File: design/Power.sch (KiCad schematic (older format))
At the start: 50 parts, among them U2 TC2117, U3 DRV8302

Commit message: Saved project with more recent version of KiCad. Added IRS2184 half bridge driver to BLDC_4_cache.lib
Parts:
- C1, C18, C19, C20, C21, C22, C23, C24, C26, C27, C28, C29, C30, C34, C36, C37, C39, C40, C43, C44, C49, C51, C52, C8, C9: symbol C -> C-RESCUE-BLDC_4
- C25, C33: symbol CP1 -> CP1-RESCUE-BLDC_4
- R15, R16, R17, R18, R19, R20, R21, R23, R24, R25, R26, R27, R32, R33, R48, R49, R50, R51: symbol R -> R-RESCUE-BLDC_4
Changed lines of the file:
@@
 EESchema Schematic File Version 2
+LIBS:BLDC_4-rescue
 LIBS:power
 LIBS:device
@@
 LIBS:crf_1
 LIBS:BLDC_4-cache
-EELAYER 24 0
+EELAYER 25 0
 EELAYER END
 $Descr A4 11693 8268
@@
 $EndDescr
 $Comp
-L C C28
+L C-RESCUE-BLDC_4 C28
 U 1 1 504F8E8D
 P 6650 3350
@@
 $EndComp
 $Comp
-L R R23
+L R-RESCUE-BLDC_4 R23
 U 1 1 504F8F6F
 P 10200 3350
@@
 $EndComp
 $Comp
-L R R24
+L R-RESCUE-BLDC_4 R24
 U 1 1 504F8F75
 P 10200 3450
@@
 $EndComp
 $Comp
-L GND #PWR048
+L GND-RESCUE-BLDC_4 #PWR048
 U 1 1 504F8F7B
 P 10700 3500
@@
 $EndComp
 $Comp
-L GND #PWR049
+L GND-RESCUE-BLDC_4 #PWR049
 U 1 1 504F8F8D
 P 10700 4000
@@
 $EndComp
 $Comp
-L R R27
+L R-RESCUE-BLDC_4 R27
 U 1 1 504F8F93
 P 10200 3950
@@
 $EndComp
 $Comp
-L R R26
+L R-RESCUE-BLDC_4 R26
 U 1 1 504F8F99
 P 10200 3850
@@
 $EndComp
 $Comp
-L R R32
+L R-RESCUE-BLDC_4 R32
 U 1 1 504F8FA3
 P 10200 4300
@@
 $EndComp
 $Comp
-L R R33
+L R-RESCUE-BLDC_4 R33
 U 1 1 504F8FA9
 P 10200 4400
@@
 $EndComp
 $Comp
-L GND #PWR050
+L GND-RESCUE-BLDC_4 #PWR050
 U 1 1 504F8FAF
 P 10700 4450
@@
 $EndComp
 $Comp
-L C C29
+L C-RESCUE-BLDC_4 C29
 U 1 1 504FA75E
 P 6650 3850
@@
 $EndComp
 $Comp
-L C C30
+L C-RESCUE-BLDC_4 C30
 U 1 1 504FA948
 P 6650 4350
@@
 NoConn ~ 6150 2650
 $Comp
-L C C26
+L C-RESCUE-BLDC_4 C26
 U 1 1 504FB6AD
 P 6450 2550
@@
 $EndComp
 $Comp
-L GND #PWR051
+L GND-RESCUE-BLDC_4 #PWR051
 U 1 1 504FB755
 P 6750 2700
@@
 $EndComp
 $Comp
-L C C27
+L C-RESCUE-BLDC_4 C27
 U 1 1 504FB924
 P 6500 2950
@@
 $EndComp
 $Comp
-L R R25
+L R-RESCUE-BLDC_4 R25
 U 1 1 504FBA6B
 P 7250 3250
@@
 $EndComp
 $Comp
-L GND #PWR052
+L GND-RESCUE-BLDC_4 #PWR052
 U 1 1 504FBA7B
 P 7600 3300
@@
 $EndComp
 $Comp
-L CP1 C33
+L CP1-RESCUE-BLDC_4 C33
 U 1 1 504FBC81
 P 8750 3250
@@
 $EndComp
 $Comp
-L GND #PWR053
+L GND-RESCUE-BLDC_4 #PWR053
 U 1 1 504FBEC1
 P 7800 3700
@@
 $EndComp
 $Comp
-L C C22
+L C-RESCUE-BLDC_4 C22
 U 1 1 504FC05A
 P 4150 3850
@@
 $EndComp
 $Comp
-L C C18
+L C-RESCUE-BLDC_4 C18
 U 1 1 504FC1DE
 P 3650 4050
@@
 $EndComp
 $Comp
-L GND #PWR055
+L GND-RESCUE-BLDC_4 #PWR055
 U 1 1 504FC2A8
 P 3650 5850
@@
 $EndComp
 $Comp
-L C C20
+L C-RESCUE-BLDC_4 C20
 U 1 1 504FC446
 P 3950 4800
@@
 $EndComp
 $Comp
-L C C23
+L C-RESCUE-BLDC_4 C23
 U 1 1 504FC64E
 P 4150 5450
@@
 $EndComp
 $Comp
-L GND #PWR056
+L GND-RESCUE-BLDC_4 #PWR056
 U 1 1 504FC918
 P 5350 5800
@@
 $EndComp
 $Comp
-L GND #PWR057
+L GND-RESCUE-BLDC_4 #PWR057
 U 1 1 504FDE04
 P 3550 3350
@@
 $EndComp
 $Comp
-L R R20
+L R-RESCUE-BLDC_4 R20
 U 1 1 504FDECB
 P 4000 3150
@@
 $EndComp
 $Comp
-L R R21
+L R-RESCUE-BLDC_4 R21
 U 1 1 504FE579
 P 4650 2200
@@
 $EndComp
 $Comp
-L GND #PWR058
+L GND-RESCUE-BLDC_4 #PWR058
 U 1 1 504FE598
 P 5000 2300
@@
 $EndComp
 $Comp
-L R R17
+L R-RESCUE-BLDC_4 R17
 U 1 1 504FE8D3
 P 3550 2200
@@
 $EndComp
 $Comp
-L R R18
+L R-RESCUE-BLDC_4 R18
 U 1 1 504FE8E8
 P 3550 2800
@@
 $EndComp
 $Comp
-L R R19
+L R-RESCUE-BLDC_4 R19
 U 1 1 504FEEA7
 P 4050 2300
@@
 $EndComp
 $Comp
-L C C21
+L C-RESCUE-BLDC_4 C21
 U 1 1 504FEEB7
 P 4050 1750
@@
 $EndComp
 $Comp
-L C C19
+L C-RESCUE-BLDC_4 C19
 U 1 1 504FEEC2
 P 3800 2050
@@
 $EndComp
 $Comp
-L R R15
+L R-RESCUE-BLDC_4 R15
 U 1 1 504FF60D
 P 3500 4700
@@
 $EndComp
 $Comp
-L R R16
+L R-RESCUE-BLDC_4 R16
 U 1 1 504FF61D
 P 3500 5350
@@
 $EndComp
 $Comp
-L C C24
+L C-RESCUE-BLDC_4 C24
 U 1 1 50500B3A
 P 6800 1400
@@
 $EndComp
 $Comp
-L GND #PWR060
+L GND-RESCUE-BLDC_4 #PWR060
 U 1 1 50500B40
 P 6300 1750
@@
 $EndComp
 $Comp
-L CP1 C25
+L CP1-RESCUE-BLDC_4 C25
 U 1 1 50500B52
 P 7200 1400
@@
 $EndComp
 $Comp
-L R R48
+L R-RESCUE-BLDC_4 R48
 U 1 1 50511A6C
 P 7250 4850
@@
 $EndComp
 $Comp
-L R R49
+L R-RESCUE-BLDC_4 R49
 U 1 1 50511A77
 P 7250 4950
@@
 $EndComp
 $Comp
-L R R50
+L R-RESCUE-BLDC_4 R50
 U 1 1 50511A82
 P 7250 5050
@@
 $EndComp
 $Comp
-L R R51
+L R-RESCUE-BLDC_4 R51
 U 1 1 50511A88
 P 7250 5150
@@
 $EndComp
 $Comp
-L C C34
+L C-RESCUE-BLDC_4 C34
 U 1 1 50511A8E
 P 6700 4950
@@
 $EndComp
 $Comp
-L C C36
+L C-RESCUE-BLDC_4 C36
 U 1 1 50511A94
 P 6700 5300
@@
 $EndComp
 $Comp
-L GND #PWR067
+L GND-RESCUE-BLDC_4 #PWR067
 U 1 1 5051337C
 P 7550 2850
@@
 NoConn ~ 4550 2950
 $Comp
-L C C39
+L C-RESCUE-BLDC_4 C39
 U 1 1 505AC7E9
 P 7250 2800
@@
 $EndComp
 $Comp
-L C C43
+L C-RESCUE-BLDC_4 C43
 U 1 1 505ACB25
 P 5900 6000
@@
 $EndComp
 $Comp
-L C C44
+L C-RESCUE-BLDC_4 C44
 U 1 1 505ACB2B
 P 5900 6250
@@
 V_SUPPLY
 $Comp
-L C C49
+L C-RESCUE-BLDC_4 C49
 U 1 1 51093C64
 P 5900 6500
@@
 $EndComp
 $Comp
-L C C51
+L C-RESCUE-BLDC_4 C51
 U 1 1 51094370
 P 9150 1500
@@
 $EndComp
 $Comp
-L GND #PWR069
+L GND-RESCUE-BLDC_4 #PWR069
 U 1 1 510944D0
 P 9700 1600
@@
 $EndComp
 $Comp
-L C C52
+L C-RESCUE-BLDC_4 C52
 U 1 1 51094BCE
 P 3950 4550
@@
 $EndComp
 $Comp
-L C C1
+L C-RESCUE-BLDC_4 C1
 U 1 1 523435A0
 P 10400 1300
@@
 $EndComp
 $Comp
-L C C37
+L C-RESCUE-BLDC_4 C37
 U 1 1 523435AB
 P 10650 1300
@@
 V_SUPPLY
 $Comp
-L C C40
+L C-RESCUE-BLDC_4 C40
 U 1 1 53E7AF97
 P 9150 1300
@@
 $EndComp
 $Comp
-L C C9
+L C-RESCUE-BLDC_4 C9
 U 1 1 53E7AFA2
 P 9150 1100
@@
 $EndComp
 $Comp
-L C C8
+L C-RESCUE-BLDC_4 C8
 U 1 1 53E7AFAD
 P 9150 900
@@
 00 FD 87 A8 17 00 00 00 00 F4 1F A2 5E 00 00 00 00 D0 7F 88 7A 01 00 00 00 40 FF 21 EA 05 00 00
 00 00 FD 87 A8 17 00 00 00 00 F4 1F A2 5E 00 00 00 00 D0 7F 88 7A 01 00 00 00 40 FF 21 EA 05 00
-00 00 00 FD F7 3F 90 37 91 24 49 74 FD E2 00 00 00 00 49 45 4E 44 AE 42 60 82 4D
+00 00 00 FD F7 3F 90 37 91 24 49 74 FD E2 00 00 00 00 49 45 4E 44 AE 42 60 82 00
 EndData
 $EndBitmap
@@
 0D 0D 85 50 5B 08 A1 71 E3 C6 45 47 47 77 AB F8 CD C0 F0 65 C3 18 9A 0F 4F 4B 4B 4B 51 51 51 53
 53 93 40 20 30 31 31 61 94 40 19 18 18 43 C3 C0 C0 A0 72 FE 07 CF 64 8C 61 E1 12 74 DD 00 00 00
-00 49 45 4E 44 AE 42 60 82 32
+00 49 45 4E 44 AE 42 60 82 93
 EndData
 $EndBitmap
@@
 20 10 88 31 C3 77 F3 62 81 40 20 10 08 04 02 81 E0 1F 14 E4 21 10 08 04 02 81 40 8C 41 50 90 87
 40 20 10 08 04 02 31 06 41 41 1E 02 81 40 20 10 08 C4 18 E4 FF 01 14 B1 03 90 4A B9 68 69 00 00
-00 00 49 45 4E 44 AE 42 60 82 4C
+00 00 49 45 4E 44 AE 42 60 82 4D
 EndData
 $EndBitmap
@@
 A1 C7 18 00 00 C0 28 C8 B2 00 00 00 46 41 96 05 00 00 30 0A B2 2C 00 00 80 51 90 65 01 00 00 8C
 82 2C 0B 00 00 60 14 64 59 00 00 00 A3 FC 7F BD 9B 69 A6 C1 67 F0 EA 00 00 00 00 49 45 4E 44 AE
-42 60 82 D7
+42 60 82 03
 EndData
 $EndBitmap
@@
 AB D8 39 0B 59 91 9E DF A8 2A 5B EE 54 3A FD 71 ED 71 2F 29 C3 82 EC 80 87 06 6E C3 98 10 30 3B
 62 9A BB 2D 03 B8 C4 64 FC B5 26 AC 13 9B D1 39 40 41 C1 D6 78 4C 84 BF 94 F0 6F E1 BF 96 F0 0F
-FF 77 E2 FF 1F 0F 43 55 32 21 1C 08 16 00 00 00 00 49 45 4E 44 AE 42 60 82 47
+FF 77 E2 FF 1F 0F 43 55 32 21 1C 08 16 00 00 00 00 49 45 4E 44 AE 42 60 82 70
 EndData
 $EndBitmap
@@
 $EndComp
 $Comp
-L GND #PWR071
+L GND-RESCUE-BLDC_4 #PWR071
 U 1 1 548EDF07
 P 8950 2200
@@
 	9550 2150 9550 2100
 $Comp
-L GND #PWR072
+L GND-RESCUE-BLDC_4 #PWR072
 U 1 1 548F3DC0
 P 10400 1650

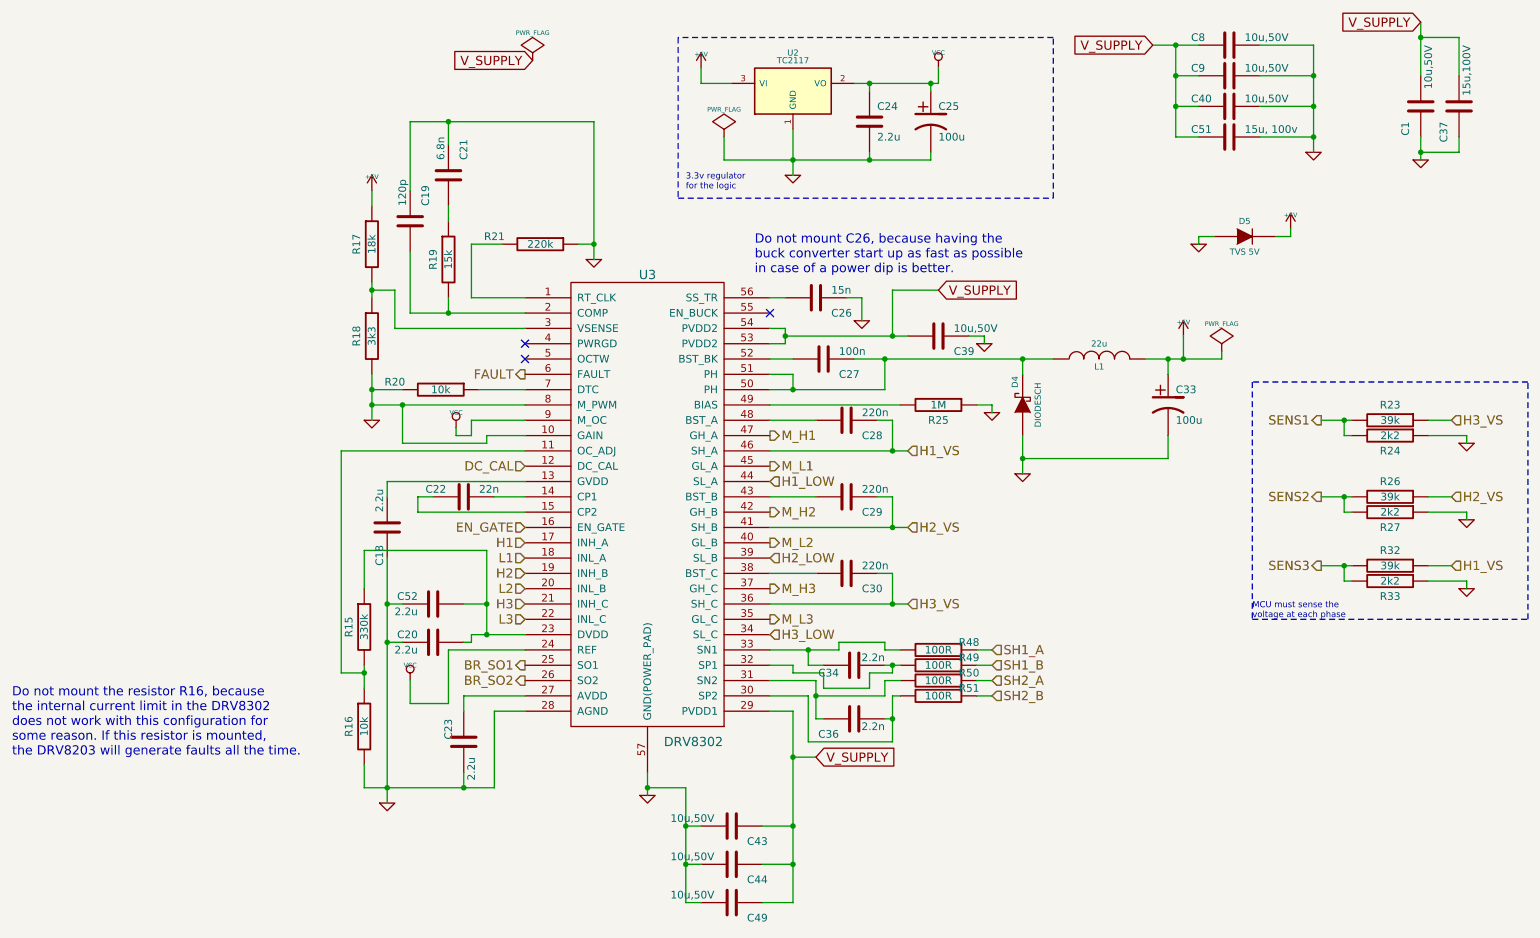
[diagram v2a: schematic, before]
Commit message: Added new drivers and removed the big old one.
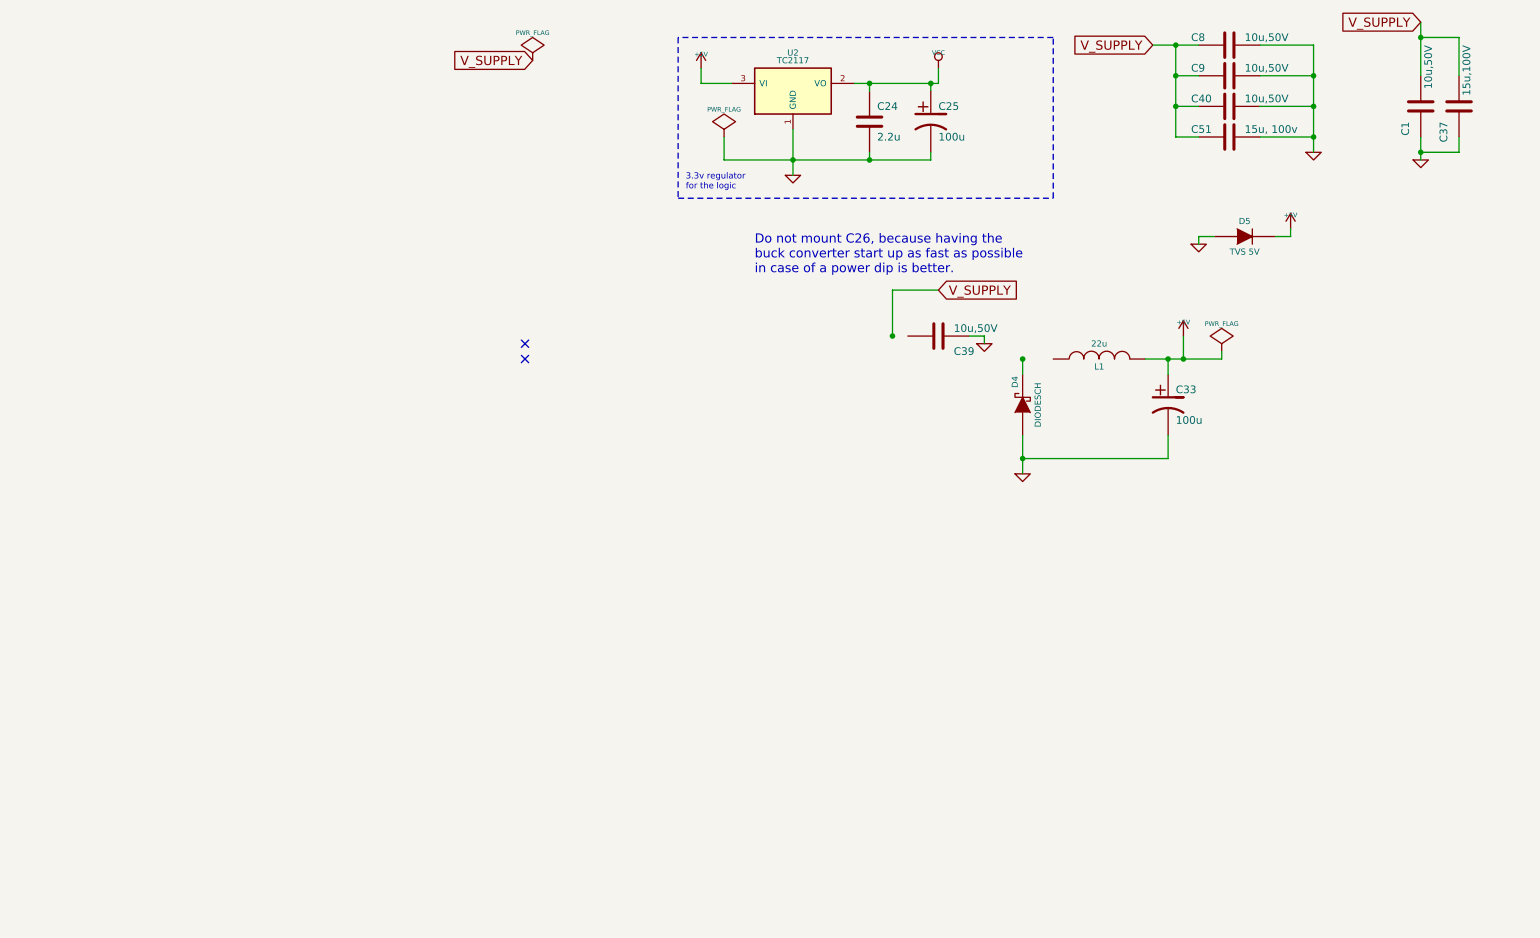
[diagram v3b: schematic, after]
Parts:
- removed C18, C23: 2.2u, SMD_Packages:SMD-0805, symbol C-RESCUE-BLDC_4
- removed C19: 120p, SMD_Packages:SMD-0603_c, symbol C-RESCUE-BLDC_4
- removed C20, C52: 2.2u, SMD_Packages:SMD-0603_c, symbol C-RESCUE-BLDC_4
- removed C21: 6.8n, SMD_Packages:SMD-0603_c, symbol C-RESCUE-BLDC_4
- removed C22: 22n, SMD_Packages:SMD-0603_c, symbol C-RESCUE-BLDC_4
- removed C26: 15n, SMD_Packages:SMD-0603_c, symbol C-RESCUE-BLDC_4
- removed C27: 100n, SMD_Packages:SMD-0603_c, symbol C-RESCUE-BLDC_4
- removed C28, C29, C30: 220n, SMD_Packages:SMD-0805, symbol C-RESCUE-BLDC_4
- removed C34, C36: 2.2n, SMD_Packages:SMD-0603_c, symbol C-RESCUE-BLDC_4
- removed C43, C44, C49: 10u,50V, SMD_Packages:SMD-1206, symbol C-RESCUE-BLDC_4
- removed R15: 330k, SMD_Packages:SMD-0603_r, symbol R-RESCUE-BLDC_4
- removed R16, R20: 10k, SMD_Packages:SMD-0603_r, symbol R-RESCUE-BLDC_4
- removed R17: 18k, SMD_Packages:SMD-0603_r, symbol R-RESCUE-BLDC_4
- removed R18: 3k3, SMD_Packages:SMD-0603_r, symbol R-RESCUE-BLDC_4
- removed R19: 15k, SMD_Packages:SMD-0603_r, symbol R-RESCUE-BLDC_4
- removed R21: 220k, SMD_Packages:SMD-0603_r, symbol R-RESCUE-BLDC_4
- removed R23, R26, R32: 39k, SMD_Packages:SMD-0603_r, symbol R-RESCUE-BLDC_4
- removed R24, R27, R33: 2k2, SMD_Packages:SMD-0603_r, symbol R-RESCUE-BLDC_4
- removed R25: 1M, SMD_Packages:SMD-0603_r, symbol R-RESCUE-BLDC_4
- removed R48, R49, R50, R51: 100R, SMD_Packages:SMD-0603_r, symbol R-RESCUE-BLDC_4
- removed U3: DRV8302, CRF1:TSSOP-56-PP, symbol DRV8302
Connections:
- net V_SUPPLY: no longer C39.2
- net at D4.2 (K): no longer L1.1
- no-connect marks 3 -> 2
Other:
- note removed: "Do not mount the resistor R16, because\nthe internal current limit in the DRV8302\ndoes not work with this configuration for\nsome reason. If this resistor is mounted, \nthe DRV8203 will generate faults all the time."
- note removed: "MCU must sense the\nvoltage at each phase"
